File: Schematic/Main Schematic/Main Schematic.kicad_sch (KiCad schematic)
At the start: 6 parts, among them J2 Conn_01x24_Socket, J2 Conn_ARM_JTAG_SWD_10, J2 USB_B_Micro, J3 Conn_01x24_Socket, SW2 SW_Push

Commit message: 'Updated'
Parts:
- removed J2: Conn_ARM_JTAG_SWD_10, symbol Connector:Conn_ARM_JTAG_SWD_10
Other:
- note added: "DEBUGGER"
- note removed: "DEBUGGER CONNECTOR"
- note removed: "This is not the actual debugger(final). Just removed from the MCU and placed it there."
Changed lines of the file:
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@@
-    (stroke (width 0) (type default))
-  )
-  (wire (pts (xy 130.81 142.24) (xy 130.81 154.94))
     (stroke (width 0) (type default))
   )
@@
     (stroke (width 0) (type default))
   )
-  (wire (pts (xy 143.51 170.18) (xy 152.4 170.18))
-    (stroke (width 0) (type default))
-  )
   (wire (pts (xy 151.2316 45.9232) (xy 151.2316 54.8132))
     (stroke (width 0) (type default))
@@
     (stroke (width 0) (type default))
   )
-  (wire (pts (xy 143.51 167.64) (xy 152.4 167.64))
-    (stroke (width 0) (type default))
-  )
   (wire (pts (xy 250.19 78.74) (xy 255.27 78.74))
     (stroke (width 0) (type default))
@@
     (stroke (width 0) (type default))
   )
-  (wire (pts (xy 143.51 162.56) (xy 152.4 162.56))
-    (stroke (width 0) (type default))
-  )
   (wire (pts (xy 207.01 45.72) (xy 207.01 50.8))
     (stroke (width 0) (type default))
@@
     (stroke (width 0) (type default))
   )
-  (wire (pts (xy 130.81 185.42) (xy 130.81 190.5))
-    (stroke (width 0) (type default))
-  )
   (wire (pts (xy 250.19 63.5) (xy 255.27 63.5))
     (stroke (width 0) (type default))
@@
   (wire (pts (xy 215.9 88.9) (xy 224.79 88.9))
     (stroke (width 0) (type default))
-  )
-  (text "This is not the actual debugger(final). Just removed from the MCU and placed it there."
-    (at 91.44 149.86 0)
-    (effects (font (size 1.27 1.27)) (justify left bottom))
   )
   (text "PIN HEADERS" (at 226.5172 21.9964 0)
     (effects (font (size 3 3)) (justify left bottom))
   )
-  (text "DEBUGGER CONNECTOR\n" (at 104.5464 136.398 0)
+  (text "DEBUGGER\n\n" (at 104.5464 136.398 0)
     (effects (font (size 3 3)) (justify left bottom))
   )
-  (label "debugger" (at 134.62 185.42 0) (fields_autoplaced)
-    (effects (font (size 1.27 1.27)) (justify left bottom))
-  )
-  (label "T_SWDIO" (at 152.4 170.18 0) (fields_autoplaced)
-    (effects (font (size 1.27 1.27)) (justify left bottom))
-  )
-  (label "NRST" (at 152.4 162.56 0) (fields_autoplaced)
-    (effects (font (size 1.27 1.27)) (justify left bottom))
-  )
-  (label "T_SWCLK" (at 152.4 167.64 0) (fields_autoplaced)
-    (effects (font (size 1.27 1.27)) (justify left bottom))
-  )
   (global_label "PC14" (shape input) (at 218.44 35.56 180) (fields_autoplaced)
     (effects (font (size 1.27 1.27)) (justify right))
@@
     (property "Intersheetrefs" "${INTERSHEET_REFS}" (at 20.32 -64.77 0)
       (effects (font (size 1.27 1.27)) hide)
-    )
-  )
-  (symbol (lib_id "power:+3V3") (at 130.81 142.24 0) (unit 1)
-    (in_bom yes) (on_board yes) (dnp no) (fields_autoplaced)
-    (property "Reference" "#PWR017" (at 130.81 146.05 0)
-      (effects (font (size 1.27 1.27)) hide)
-    )
-    (property "Value" "+3V3" (at 130.81 138.43 0)
-      (effects (font (size 1.27 1.27)))
-    )
-    (property "Footprint" "" (at 130.81 142.24 0)
-      (effects (font (size 1.27 1.27)) hide)
-    )
-    (property "Datasheet" "" (at 130.81 142.24 0)
-      (effects (font (size 1.27 1.27)) hide)
-    )
-    (pin "1")
-    (instances
-      (project "Main Schematic"
-        (path "/81c41bad-bb43-41af-b405-18d135a809b1/ae15d31d-f7b4-4051-b9d0-3a01939afe0e"
-          (reference "#PWR017") (unit 1)
-        )
-        (path "/81c41bad-bb43-41af-b405-18d135a809b1"
-          (reference "#PWR017") (unit 1)
-        )
-      )
-      (project "Microcontroller Design"
-        (path "/b8d97438-63f4-433e-afdc-8e43ab7e4842"
-          (reference "#PWR06") (unit 1)
-        )
-      )
-      (project "MCU"
-        (path "/e0666d22-e687-4adb-b95b-6588526d91f1"
-          (reference "#PWR07") (unit 1)
-        )
-      )
     )
   )
@@
         )
       )
-    )
-  )
-  (symbol (lib_id "Connector:Conn_ARM_JTAG_SWD_10") (at 130.81 170.18 0) (unit 1)
-    (in_bom yes) (on_board yes) (dnp no) (fields_autoplaced)
-    (property "Reference" "J2" (at 119.38 169.545 0)
-      (effects (font (size 1.27 1.27)) (justify right))
-    )
-    (property "Value" "Conn_ARM_JTAG_SWD_10" (at 119.38 172.085 0)
-      (effects (font (size 1.27 1.27)) (justify right))
-    )
-    (property "Footprint" "" (at 130.81 170.18 0)
-      (effects (font (size 1.27 1.27)) hide)
-    )
-    (property "Datasheet" "http://infocenter.arm.com/help/topic/com.arm.doc.ddi0314h/DDI0314H_coresight_components_trm.pdf" (at 121.92 201.93 90)
-      (effects (font (size 1.27 1.27)) hide)
-    )
-    (pin "1")
-    (pin "10")
-    (pin "2")
-    (pin "3")
-    (pin "4")
-    (pin "5")
-    (pin "6")
-    (pin "7")
-    (pin "8")
-    (pin "9")
-    (instances
-      (project "Main Schematic"
-        (path "/81c41bad-bb43-41af-b405-18d135a809b1/ae15d31d-f7b4-4051-b9d0-3a01939afe0e"
-          (reference "J2") (unit 1)
-        )
-        (path "/81c41bad-bb43-41af-b405-18d135a809b1"
-          (reference "J4") (unit 1)
-        )
-      )
-      (project "Microcontroller Design"
-        (path "/b8d97438-63f4-433e-afdc-8e43ab7e4842"
-          (reference "J1") (unit 1)
-        )
-      )
-      (project "MCU"
-        (path "/e0666d22-e687-4adb-b95b-6588526d91f1"
-          (reference "J3") (unit 1)
-        )
-      )
-    )
-  )
-  (symbol (lib_id "power:GND") (at 130.81 190.5 0) (unit 1)
-    (in_bom yes) (on_board yes) (dnp no) (fields_autoplaced)
-    (property "Reference" "#PWR018" (at 130.81 196.85 0)
-      (effects (font (size 1.27 1.27)) hide)
-    )
-    (property "Value" "GND" (at 130.81 195.58 0)
-      (effects (font (size 1.27 1.27)))
-    )
-    (property "Footprint" "" (at 130.81 190.5 0)
-      (effects (font (size 1.27 1.27)) hide)
-    )
-    (property "Datasheet" "" (at 130.81 190.5 0)
-      (effects (font (size 1.27 1.27)) hide)
-    )
-    (pin "1")
-    (instances
-      (project "Main Schematic"
-        (path "/81c41bad-bb43-41af-b405-18d135a809b1/ae15d31d-f7b4-4051-b9d0-3a01939afe0e"
-          (reference "#PWR018") (unit 1)
-        )
-        (path "/81c41bad-bb43-41af-b405-18d135a809b1"
-          (reference "#PWR018") (unit 1)
-        )
-      )
-      (project "Microcontroller Design"
-        (path "/b8d97438-63f4-433e-afdc-8e43ab7e4842"
-          (reference "#PWR07") (unit 1)
-        )
-      )
-      (project "MCU"
-        (path "/e0666d22-e687-4adb-b95b-6588526d91f1"
-          (reference "#PWR08") (unit 1)
-        )
-      )

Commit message: 'Update'
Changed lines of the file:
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@@
+    (stroke (width 0) (type default))
+  )
+  (wire (pts (xy 147.32 35.56) (xy 162.56 35.56))
     (stroke (width 0) (type default))
   )
@@
     (effects (font (size 3 3)) (justify left bottom))
   )
+  (global_label "Vcc 5V" (shape input) (at 162.56 35.56 0) (fields_autoplaced)
+    (effects (font (size 1.27 1.27)) (justify left))
+    (property "Intersheetrefs" "${INTERSHEET_REFS}" (at 171.7917 35.56 0)
+      (effects (font (size 1.27 1.27)) (justify left) hide)
+    )
+  )
   (global_label "PC14" (shape input) (at 218.44 35.56 180) (fields_autoplaced)

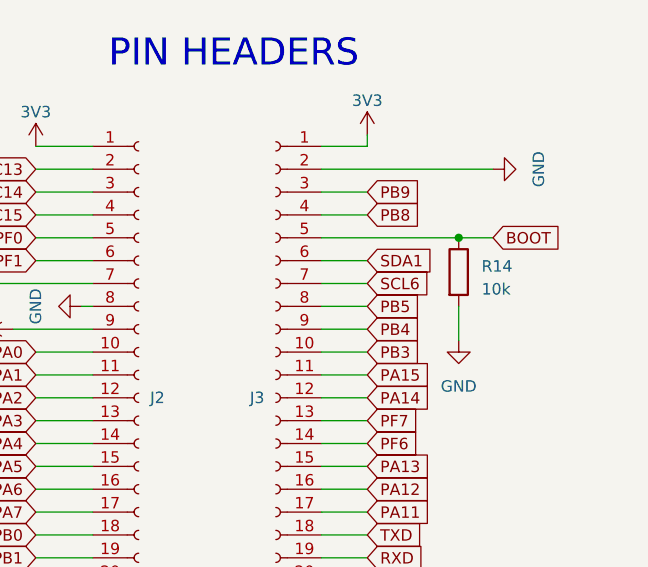
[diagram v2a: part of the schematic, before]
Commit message: I have commented on my module explaining the significant parts
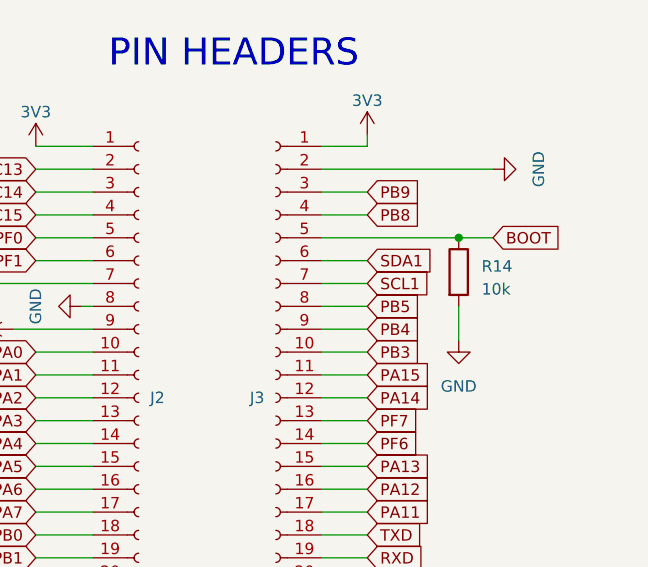
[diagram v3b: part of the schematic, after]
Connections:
- net SCL6 renamed SCL1
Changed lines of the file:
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@@
     )
   )
-  (global_label "SCL6" (shape input) (at 255.27 45.72 0) (fields_autoplaced)
+  (global_label "SCL1" (shape input) (at 255.27 45.72 0) (fields_autoplaced)
     (effects (font (size 1.27 1.27)) (justify left))
     (property "Intersheetrefs" "${INTERSHEET_REFS}" (at 262.8929 45.72 0)

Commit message: 'Updated'
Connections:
- net PB10 renamed SCL2
- net PB11 renamed SDA2
- net PB12 renamed Write1
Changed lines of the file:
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@@
     )
   )
-  (global_label "PB12" (shape input) (at 255.27 88.9 0) (fields_autoplaced)
+  (global_label "Write1" (shape input) (at 255.27 88.9 0) (fields_autoplaced)
     (effects (font (size 1.27 1.27)) (justify left))
-    (property "Intersheetrefs" "${INTERSHEET_REFS}" (at 20.32 -64.77 0)
-      (effects (font (size 1.27 1.27)) hide)
+    (property "Intersheetrefs" "${INTERSHEET_REFS}" (at 264.042 88.9 0)
+      (effects (font (size 1.27 1.27)) (justify left) hide)
     )
   )
@@
     )
   )
-  (global_label "PB11" (shape input) (at 218.44 83.82 180) (fields_autoplaced)
+  (global_label "SDA2" (shape input) (at 218.44 83.82 180) (fields_autoplaced)
     (effects (font (size 1.27 1.27)) (justify right))
-    (property "Intersheetrefs" "${INTERSHEET_REFS}" (at 20.32 -64.77 0)
-      (effects (font (size 1.27 1.27)) hide)
+    (property "Intersheetrefs" "${INTERSHEET_REFS}" (at 210.7566 83.82 0)
+      (effects (font (size 1.27 1.27)) (justify right) hide)
     )
   )
@@
     )
   )
-  (global_label "PB10" (shape input) (at 218.44 81.28 180) (fields_autoplaced)
+  (global_label "SCL2" (shape input) (at 218.44 81.28 180) (fields_autoplaced)
     (effects (font (size 1.27 1.27)) (justify right))
-    (property "Intersheetrefs" "${INTERSHEET_REFS}" (at 20.32 -64.77 0)
-      (effects (font (size 1.27 1.27)) hide)
+    (property "Intersheetrefs" "${INTERSHEET_REFS}" (at 210.8171 81.28 0)
+      (effects (font (size 1.27 1.27)) (justify right) hide)
     )
   )

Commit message: 'update'
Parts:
- added J7: Conn_01x10_Pin, symbol Connector:Conn_01x10_Pin
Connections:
- net GND: now also J7.1 (Pin_1)
- net RXD: now also J7.2 (Pin_2)
- net SCL1: now also J7.7 (Pin_7)
- net SCL2: now also J7.5 (Pin_5)
- net SDA1: now also J7.8 (Pin_8)
- net SDA2: now also J7.6 (Pin_6)
- net TXD: now also J7.3 (Pin_3)
- new net +5V: J7.10 (Pin_10)
- new net ADC1: J7.9 (Pin_9)
- new net write1: J7.4 (Pin_4)
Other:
- note added: "Connectors"
- note removed: "DEBUGGER"

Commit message: 'Update'
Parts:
- renumbered J7 to J1
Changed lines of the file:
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@@
   (symbol (lib_id "Connector:Conn_01x10_Pin") (at 128.27 163.83 180) (unit 1)
     (in_bom yes) (on_board yes) (dnp no) (fields_autoplaced)
-    (property "Reference" "J7" (at 129.54 161.925 0)
+    (property "Reference" "J1" (at 129.54 161.925 0)
       (effects (font (size 1.27 1.27)) (justify right))
     )
@@
       (project "Main Schematic"
         (path "/81c41bad-bb43-41af-b405-18d135a809b1"
-          (reference "J7") (unit 1)
+          (reference "J1") (unit 1)
         )
       )

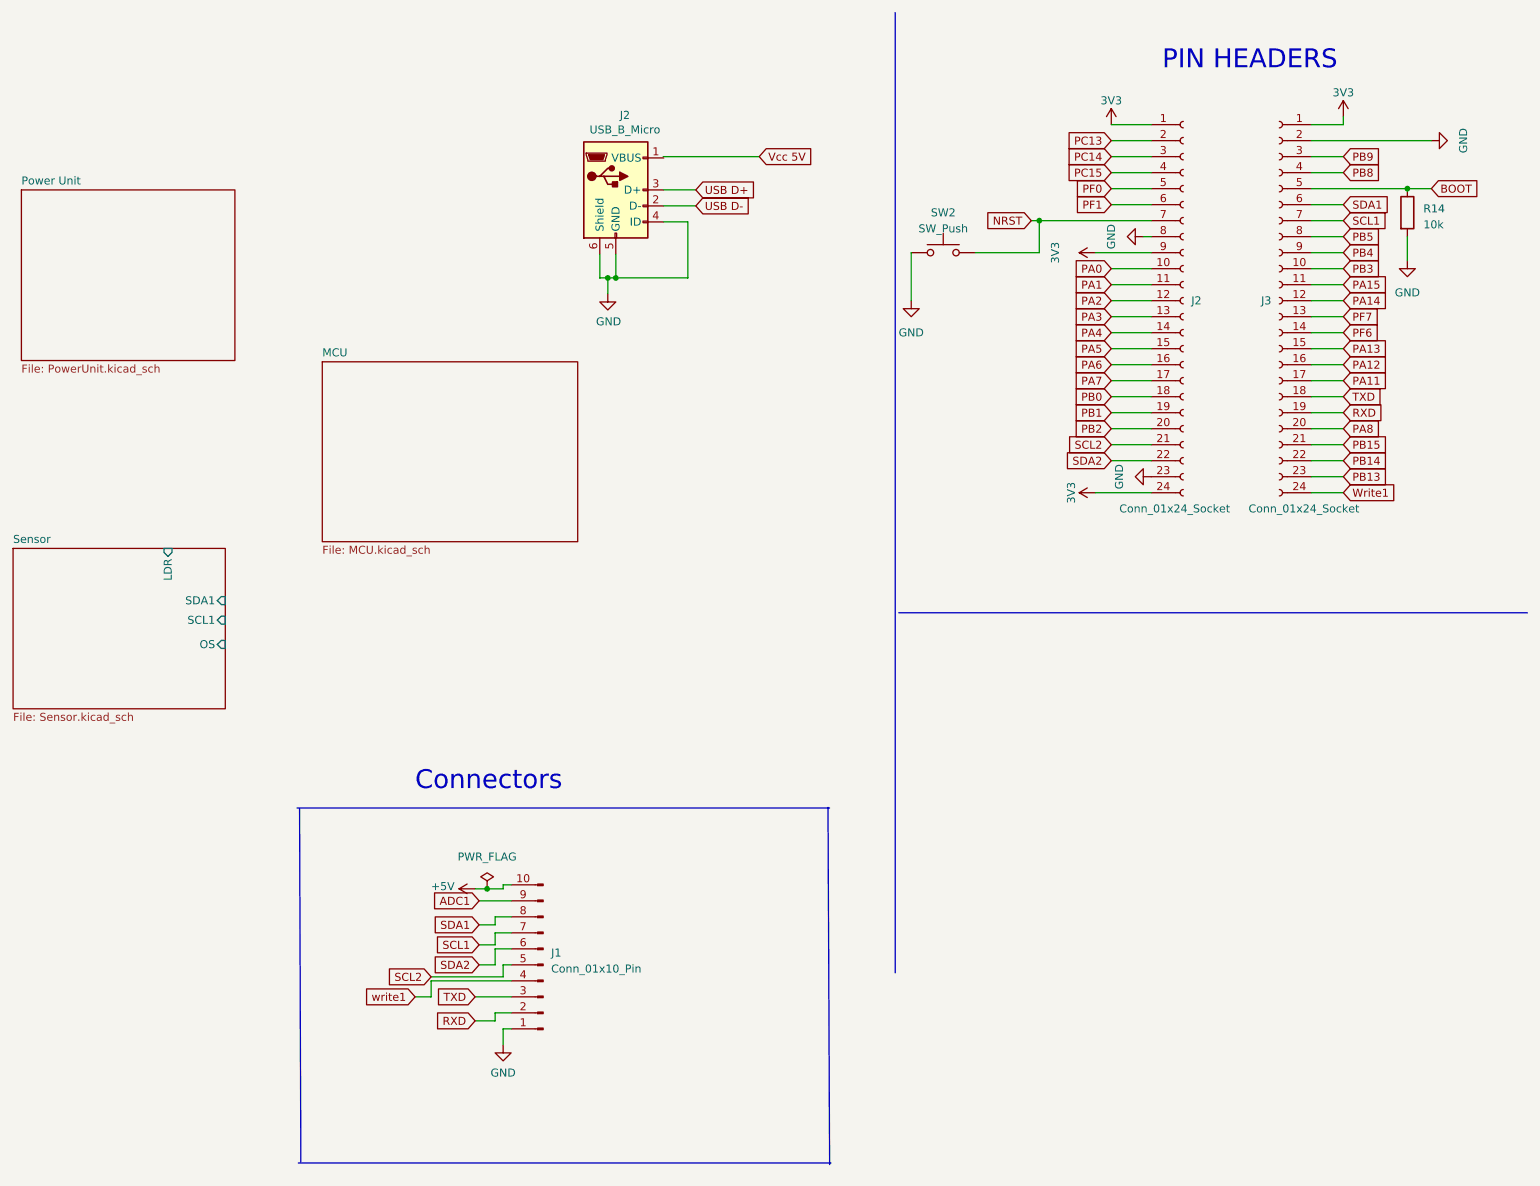
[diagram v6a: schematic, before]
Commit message: I have added net lables and hierachy labels on the main schmeatic
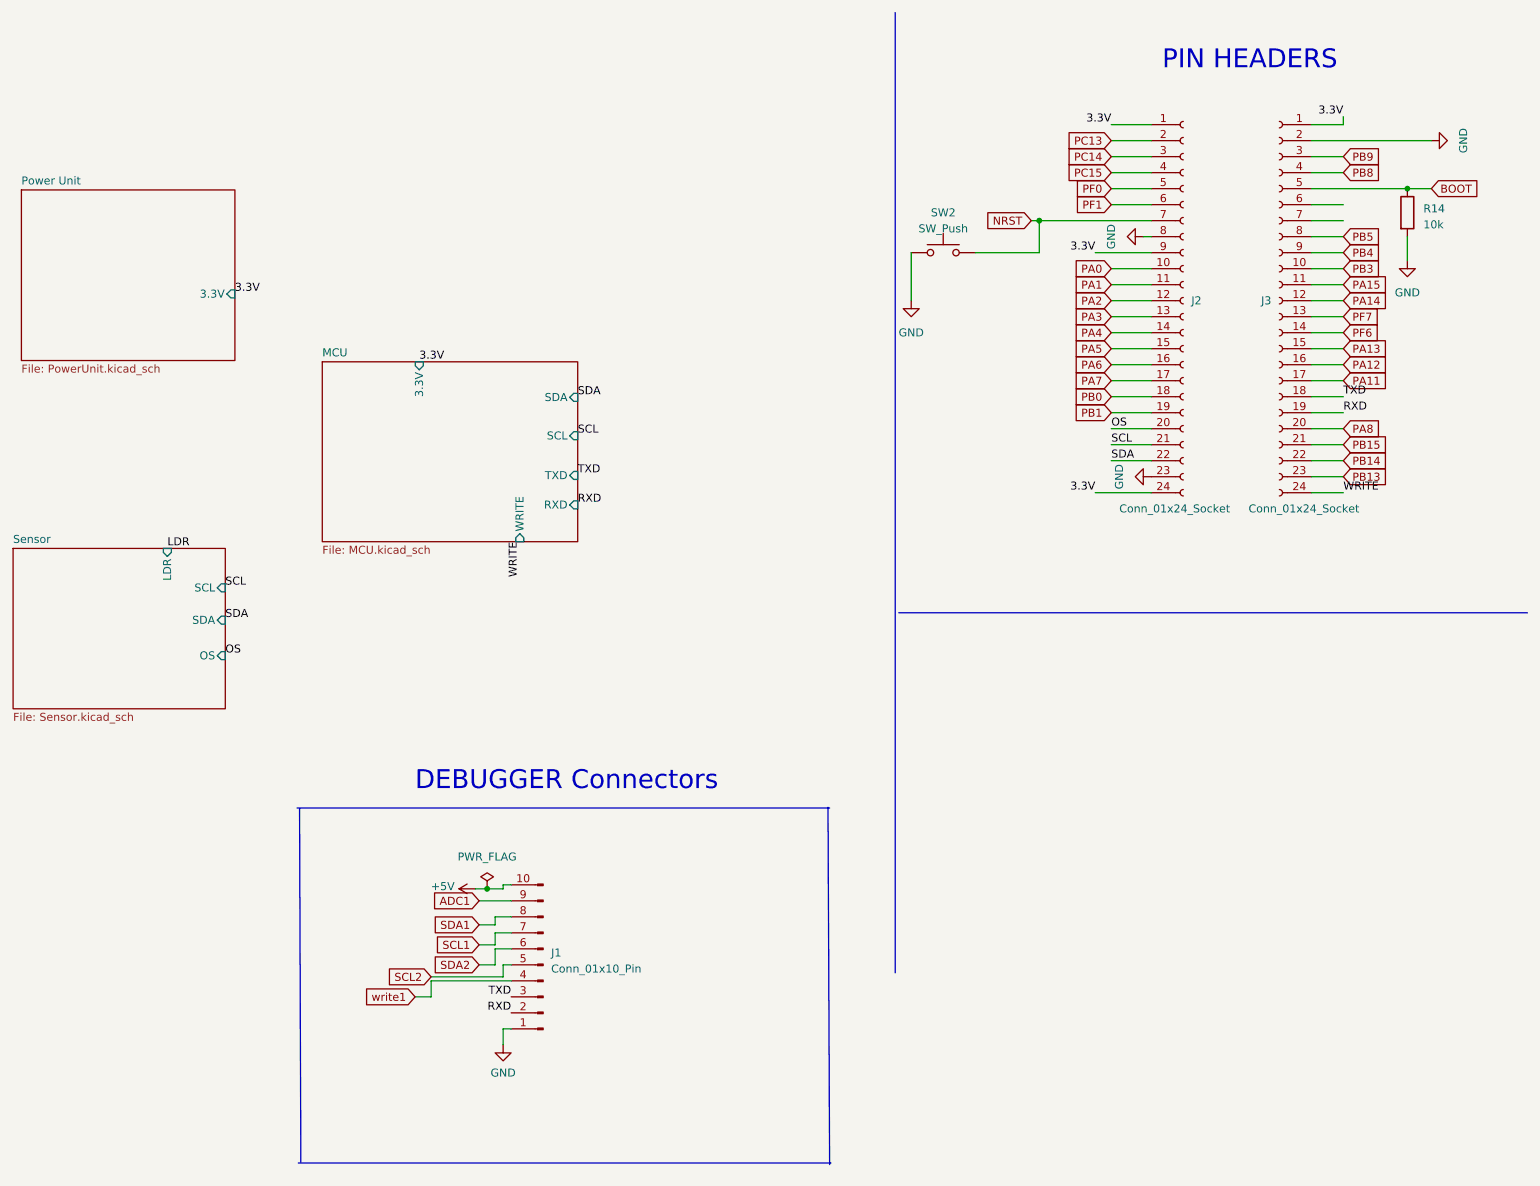
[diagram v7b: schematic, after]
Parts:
- removed J2: USB_B_Micro, symbol Connector:USB_B_Micro
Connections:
- net SCL1: no longer J3.7 (Pin_7)
- net SCL2: no longer J2.21 (Pin_21)
- net SDA1: no longer J3.6 (Pin_6)
- net SDA2: no longer J2.22 (Pin_22)
- net PB2 renamed OS
- net VCC renamed 3.3V
- net Write1 renamed WRITE
- new net SCL: J2.21 (Pin_21)
- new net SDA: J2.22 (Pin_22)
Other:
- sheet MCU ports: added 3.3V, RXD, SCL, SDA, TXD, WRITE; removed none
- sheet Power Unit ports: added 3.3V; removed none
- sheet Sensor ports: added SCL, SDA; removed SCL1, SDA1
- note added: "DEBUGGER Connectors"
- note removed: "Connectors"
- company: (none) -> UCT
- title: (none) -> MAIN SCHEMATIC

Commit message: Update
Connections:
- net ADC1 is gone; now on net +5V: J1.9 (Pin_9)
- net PB0 is gone; now on net LDR: J2.18 (Pin_18)
- net SCL1 is gone; now on net LDR: J1.7 (Pin_7)
- net SCL2 is gone; now on net SCL: J1.5 (Pin_5)
- net SDA1 is gone; now on net 3.3V: J1.8 (Pin_8)
- net SDA2 is gone; now on net SDA: J1.6 (Pin_6)
- net write1 is gone; now on net WRITE: J1.4 (Pin_4)
- net +5V: no longer J1.10 (Pin_10)
- net PA7 renamed P07
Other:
- sheet Sensor ports: added 3.3V; removed none
